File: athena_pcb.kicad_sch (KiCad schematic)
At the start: 34 parts, among them J2 Conn_01x04, SW1 SW_Push, U1 NRF5340-QKAA-R7, U2 BME280, Y1 32MHz, Y2 32.768kHz

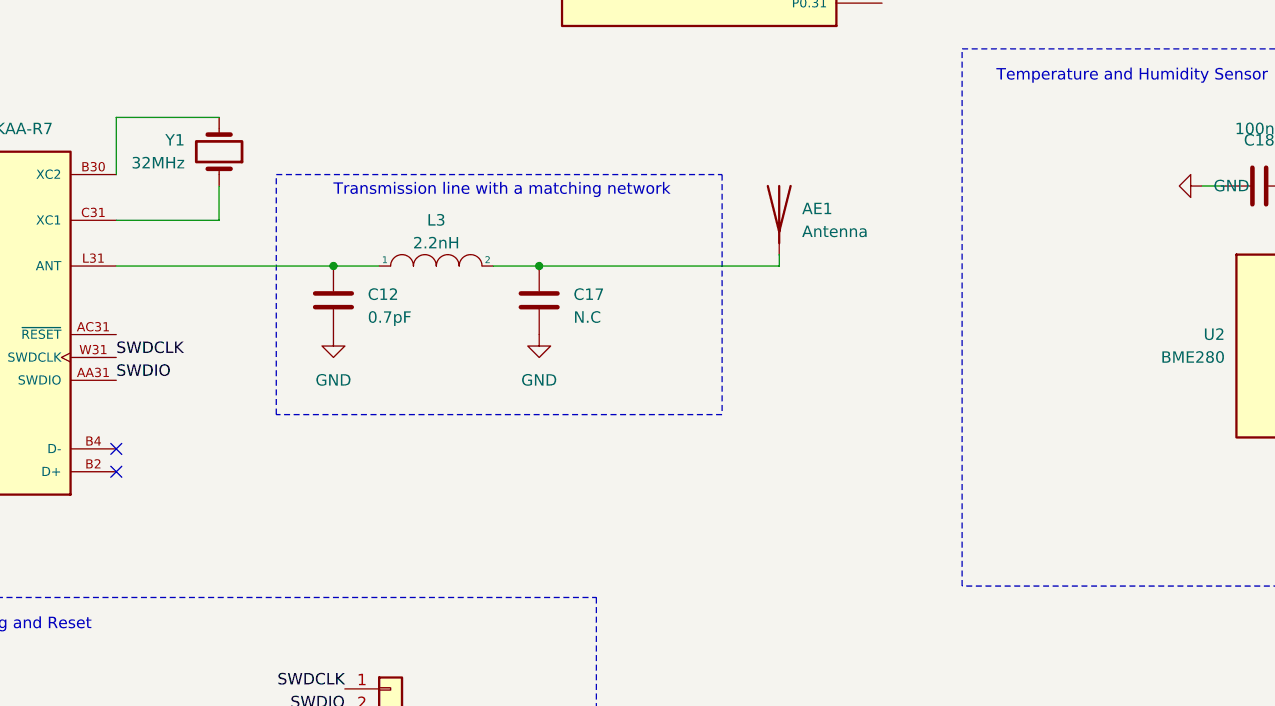
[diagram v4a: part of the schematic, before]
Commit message: Adapted PCB antenna footprint to use polygon, Workaroung for schematic symbol
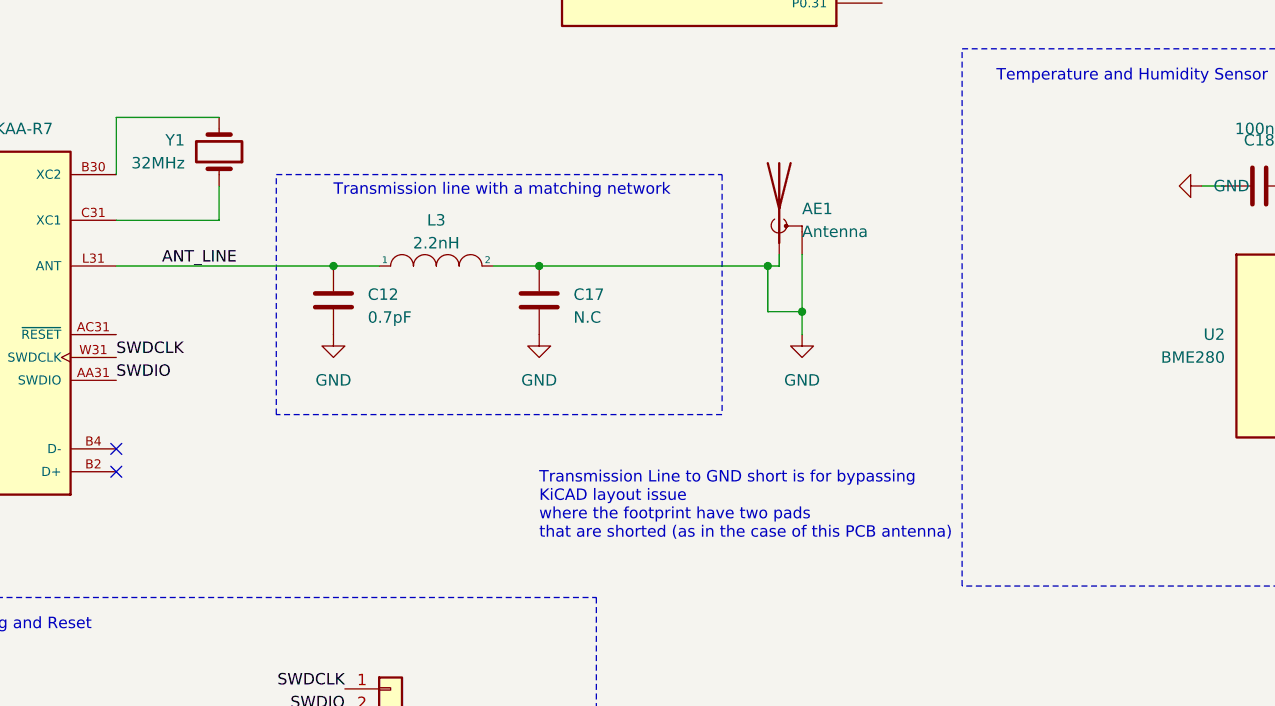
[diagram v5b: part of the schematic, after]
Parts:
- AE1: footprint RF_Antenna:Texas_SWRA117D_2.4GHz_Left -> RF_Antenna:Texas_SWRA117D_2.4GHz_Right; symbol Device:Antenna -> Device:Antenna_Shield
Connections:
- net GND: now also AE1.1 (A), AE1.2 (Shield), C17.1, L3.2
- net ANT_LINE: now reaches C12.1, L3.1, U1.L31 (ANT)
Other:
- note added: "Transmission Line to GND short is for bypassing KiCAD layout issue where the footprint have two pads that are shorted (as in the case of this PCB antenna)"
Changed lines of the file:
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@@
   (junction (at 52.07 40.64) (diameter 0) (color 0 0 0 0)
   )
+  (junction (at 191.77 133.35) (diameter 0) (color 0 0 0 0)
+  )
   (junction (at 111.76 27.94) (diameter 0) (color 0 0 0 0)
   )
@@
   )
   (junction (at 76.2 35.56) (diameter 0) (color 0 0 0 0)
+  )
+  (junction (at 187.96 128.27) (diameter 0) (color 0 0 0 0)
   )
   (junction (at 111.76 68.58) (diameter 0) (color 0 0 0 0)
@@
     (stroke (width 0) (type default))
   )
+  (wire (pts (xy 191.77 127) (xy 191.77 133.35))
+    (stroke (width 0) (type default))
+  )
   (wire (pts (xy 127 119.38) (xy 127 123.19))
     (stroke (width 0) (type default))
@@
     (stroke (width 0) (type default))
   )
+  (wire (pts (xy 187.96 133.35) (xy 191.77 133.35))
+    (stroke (width 0) (type default))
+  )
   (wire (pts (xy 69.85 68.58) (xy 69.85 69.85))
     (stroke (width 0) (type default))
@@
     (stroke (width 0) (type default))
   )
+  (wire (pts (xy 191.77 133.35) (xy 191.77 135.89))
+    (stroke (width 0) (type default))
+  )
   (wire (pts (xy 250.19 118.11) (xy 252.73 118.11))
     (stroke (width 0) (type default))
@@
     (stroke (width 0) (type default))
   )
+  (wire (pts (xy 187.96 128.27) (xy 189.23 128.27))
+    (stroke (width 0) (type default))
+  )
+  (wire (pts (xy 187.96 128.27) (xy 187.96 133.35))
+    (stroke (width 0) (type default))
+  )
   (wire (pts (xy 232.41 85.09) (xy 228.6 85.09))
     (stroke (width 0) (type default))
@@
     (stroke (width 0) (type default))
   )
-  (wire (pts (xy 162.56 128.27) (xy 189.23 128.27))
+  (wire (pts (xy 162.56 128.27) (xy 187.96 128.27))
     (stroke (width 0) (type default))
   )
@@
     (effects (font (size 1.27 1.27)) (justify left bottom))
   )
+  (text "Transmission Line to GND short is for bypassing\nKiCAD layout issue\nwhere the footprint have two pads\nthat are shorted (as in the case of this PCB antenna)\n"
+    (at 162.56 158.75 0)
+    (effects (font (size 1.27 1.27)) (justify left bottom))
+  )
   (label "SDO" (at 265.43 129.54 0) (fields_autoplaced)
     (effects (font (size 1.27 1.27)) (justify left bottom))
@@
   )
   (label "P0.02" (at 200.66 25.4 0) (fields_autoplaced)
+    (effects (font (size 1.27 1.27)) (justify left bottom))
+  )
+  (label "ANT_LINE" (at 120.65 128.27 0) (fields_autoplaced)
     (effects (font (size 1.27 1.27)) (justify left bottom))
   )
@@
         (path "/fadb6411-1081-41a3-ba72-837bcce93ee0"
           (reference "U2") (unit 1)
+        )
+      )
+    )
+  )
+  (symbol (lib_id "power:GND") (at 191.77 135.89 0) (unit 1)
+    (in_bom yes) (on_board yes) (dnp no) (fields_autoplaced)
+    (property "Reference" "#PWR06" (at 191.77 142.24 0)
+      (effects (font (size 1.27 1.27)) hide)
+    )
+    (property "Value" "GND" (at 191.77 140.97 0)
+      (effects (font (size 1.27 1.27)))
+    )
+    (property "Footprint" "" (at 191.77 135.89 0)
+      (effects (font (size 1.27 1.27)) hide)
+    )
+    (property "Datasheet" "" (at 191.77 135.89 0)
+      (effects (font (size 1.27 1.27)) hide)
+    )
+    (pin "1")
+    (instances
+      (project "athena_pcb"
+        (path "/fadb6411-1081-41a3-ba72-837bcce93ee0"
+          (reference "#PWR06") (unit 1)
         )
       )
@@
     )
   )
-  (symbol (lib_id "Device:Antenna") (at 189.23 121.92 0) (unit 1)
+  (symbol (lib_id "Device:Antenna_Shield") (at 189.23 121.92 0) (unit 1)
     (in_bom yes) (on_board yes) (dnp no) (fields_autoplaced)
     (property "Reference" "AE1" (at 191.77 121.92 0)
@@
       (effects (font (size 1.27 1.27)) (justify left))
     )
-    (property "Footprint" "RF_Antenna:Texas_SWRA117D_2.4GHz_Left" (at 189.23 121.92 0)
-      (effects (font (size 1.27 1.27)) hide)
-    )
-    (property "Datasheet" "~" (at 189.23 121.92 0)
-      (effects (font (size 1.27 1.27)) hide)
-    )
-    (pin "1")
-    (instances
-      (project "athena_pcb"
+    (property "Footprint" "RF_Antenna:Texas_SWRA117D_2.4GHz_Right" (at 189.23 119.38 0)
+      (effects (font (size 1.27 1.27)) hide)
+    )
+    (property "Datasheet" "~" (at 189.23 119.38 0)
+      (effects (font (size 1.27 1.27)) hide)
+    )
+    (pin "1")
+    (pin "2")
+    (instances
+      (project "athena_pcb"

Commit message: Added proper Y1 symbol and footprint
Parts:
- removed Y1: 32MHz, Crystal:Crystal_SMD_2016-4Pin_2.0x1.6mm, symbol Device:Crystal
- added Y1: 32MHz, XRCGB32M000F1H19R0:OSC_XRCGB32M000F1H19R0, symbol XRCGB32M000F1H19R0:XRCGB32M000F1H19R0
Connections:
- net at U1.C31 (XC1): now also Y1.3
- net at U1.B30 (XC2): now also Y1.1
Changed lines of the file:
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@@
-    (stroke (width 0) (type default))
-  )
-  (wire (pts (xy 127 119.38) (xy 127 123.19))
     (stroke (width 0) (type default))
   )
@@
     (stroke (width 0) (type default))
   )
+  (wire (pts (xy 242.57 86.36) (xy 242.57 83.82))
+    (stroke (width 0) (type default))
+  )
+  (wire (pts (xy 111.76 68.58) (xy 111.76 71.12))
+    (stroke (width 0) (type default))
+  )
+  (wire (pts (xy 60.96 45.72) (xy 76.2 45.72))
+    (stroke (width 0) (type default))
+  )
+  (wire (pts (xy 187.96 128.27) (xy 189.23 128.27))
+    (stroke (width 0) (type default))
+  )
+  (wire (pts (xy 187.96 128.27) (xy 187.96 133.35))
+    (stroke (width 0) (type default))
+  )
+  (wire (pts (xy 232.41 85.09) (xy 228.6 85.09))
+    (stroke (width 0) (type default))
+  )
+  (wire (pts (xy 236.22 119.38) (xy 238.76 119.38))
+    (stroke (width 0) (type default))
+  )
+  (wire (pts (xy 20.32 25.4) (xy 20.32 27.94))
+    (stroke (width 0) (type default))
+  )
+  (wire (pts (xy 261.62 119.38) (xy 264.16 119.38))
+    (stroke (width 0) (type default))
+  )
+  (wire (pts (xy 250.19 152.4) (xy 252.73 152.4))
+    (stroke (width 0) (type default))
+  )
+  (wire (pts (xy 139.7 128.27) (xy 144.78 128.27))
+    (stroke (width 0) (type default))
+  )
+  (wire (pts (xy 162.56 128.27) (xy 187.96 128.27))
+    (stroke (width 0) (type default))
+  )
   (wire (pts (xy 115.57 111.76) (xy 127 111.76))
     (stroke (width 0) (type default))
   )
-  (wire (pts (xy 242.57 86.36) (xy 242.57 83.82))
-    (stroke (width 0) (type default))
-  )
-  (wire (pts (xy 111.76 68.58) (xy 111.76 71.12))
-    (stroke (width 0) (type default))
-  )
-  (wire (pts (xy 60.96 45.72) (xy 76.2 45.72))
-    (stroke (width 0) (type default))
-  )
-  (wire (pts (xy 187.96 128.27) (xy 189.23 128.27))
-    (stroke (width 0) (type default))
-  )
-  (wire (pts (xy 187.96 128.27) (xy 187.96 133.35))
-    (stroke (width 0) (type default))
-  )
-  (wire (pts (xy 232.41 85.09) (xy 228.6 85.09))
-    (stroke (width 0) (type default))
-  )
-  (wire (pts (xy 236.22 119.38) (xy 238.76 119.38))
-    (stroke (width 0) (type default))
-  )
-  (wire (pts (xy 20.32 25.4) (xy 20.32 27.94))
-    (stroke (width 0) (type default))
-  )
-  (wire (pts (xy 261.62 119.38) (xy 264.16 119.38))
-    (stroke (width 0) (type default))
-  )
-  (wire (pts (xy 250.19 152.4) (xy 252.73 152.4))
-    (stroke (width 0) (type default))
-  )
-  (wire (pts (xy 139.7 128.27) (xy 144.78 128.27))
-    (stroke (width 0) (type default))
-  )
-  (wire (pts (xy 162.56 128.27) (xy 187.96 128.27))
-    (stroke (width 0) (type default))
-  )
   (wire (pts (xy 68.58 55.88) (xy 76.2 55.88))
     (stroke (width 0) (type default))
@@
   )
   (wire (pts (xy 252.73 119.38) (xy 252.73 121.92))
+    (stroke (width 0) (type default))
+  )
+  (wire (pts (xy 127 121.92) (xy 127 123.19))
     (stroke (width 0) (type default))
   )
@@
     )
   )
+  (symbol (lib_id "XRCGB32M000F1H19R0:XRCGB32M000F1H19R0") (at 127 116.84 270) (unit 1)
+    (in_bom yes) (on_board yes) (dnp no) (fields_autoplaced)
+    (property "Reference" "Y1" (at 130.81 116.205 90)
+      (effects (font (size 1.27 1.27)) (justify left))
+    )
+    (property "Value" "32MHz" (at 130.81 118.745 90)
+      (effects (font (size 1.27 1.27)) (justify left))
+    )
+    (property "Footprint" "XRCGB32M000F1H19R0:OSC_XRCGB32M000F1H19R0" (at 127 116.84 0)
+      (effects (font (size 1.27 1.27)) (justify bottom) hide)
+    )
+    (property "Datasheet" "" (at 127 116.84 0)
+      (effects (font (size 1.27 1.27)) hide)
+    )
+    (property "MANUFACTURER" "Murata Electronics" (at 127 116.84 0)
+      (effects (font (size 1.27 1.27)) (justify bottom) hide)
+    )
+    (property "PARTREV" "N/A" (at 127 116.84 0)
+      (effects (font (size 1.27 1.27)) (justify bottom) hide)
+    )
+    (property "MAXIMUM_PACKAGE_HEIGHT" "0.7 mm" (at 127 116.84 0)
+      (effects (font (size 1.27 1.27)) (justify bottom) hide)
+    )
+    (property "STANDARD" "Manufacturer Recommendations" (at 127 116.84 0)
+      (effects (font (size 1.27 1.27)) (justify bottom) hide)
+    )
+    (pin "1")
+    (pin "3")
+    (instances
+      (project "athena_pcb"
+        (path "/fadb6411-1081-41a3-ba72-837bcce93ee0"
+          (reference "Y1") (unit 1)
+        )
+      )
+    )
+  )
   (symbol (lib_id "NRF5340-QKAA-R7:NRF5340-QKAA-R7") (at 180.34 58.42 0) (mirror y) (unit 3)
     (in_bom yes) (on_board yes) (dnp no) (fields_autoplaced)
@@
         )
       )
-    )
-  )
-  (symbol (lib_id "Device:Crystal") (at 127 115.57 270) (mirror x) (unit 1)
-    (in_bom yes) (on_board yes) (dnp no) (fields_autoplaced)
-    (property "Reference" "Y1" (at 123.19 114.2999 90)
-      (effects (font (size 1.27 1.27)) (justify right))
-    )
-    (property "Value" "32MHz" (at 123.19 116.8399 90)
-      (effects (font (size 1.27 1.27)) (justify right))
-    )
-    (property "Footprint" "Crystal:Crystal_SMD_2016-4Pin_2.0x1.6mm" (at 127 115.57 0)
-      (effects (font (size 1.27 1.27)) hide)
-    )
-    (property "Datasheet" "~" (at 127 115.57 0)
-      (effects (font (size 1.27 1.27)) hide)
-    )
-    (pin "1")
-    (pin "2")
-    (instances
-      (project "athena_pcb"
-        (path "/fadb6411-1081-41a3-ba72-837bcce93ee0"
-          (reference "Y1") (unit 1)
-        )
-      )

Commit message: Polishing layout
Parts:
- added TP3, TP4: TestPoint, TestPoint:TestPoint_Pad_D1.0mm, symbol Connector:TestPoint
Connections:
- net CSB: now also TP4.1
- net SDO: now also TP3.1
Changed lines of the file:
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@@
+    (stroke (width 0) (type default))
+  )
+  (wire (pts (xy 228.6 95.25) (xy 228.6 93.98))
     (stroke (width 0) (type default))
   )
@@
     (stroke (width 0) (type default))
   )
+  (wire (pts (xy 247.65 95.25) (xy 243.84 95.25))
+    (stroke (width 0) (type default))
+  )
   (wire (pts (xy 31.75 101.6) (xy 31.75 104.14))
     (stroke (width 0) (type default))
@@
     (stroke (width 0) (type default))
   )
+  (wire (pts (xy 228.6 95.25) (xy 233.68 95.25))
+    (stroke (width 0) (type default))
+  )
   (wire (pts (xy 261.62 119.38) (xy 264.16 119.38))
+    (stroke (width 0) (type default))
+  )
+  (wire (pts (xy 243.84 95.25) (xy 243.84 92.71))
     (stroke (width 0) (type default))
   )
@@
     (effects (font (size 1.27 1.27)) (justify left bottom))
   )
+  (label "CSB" (at 247.65 95.25 0) (fields_autoplaced)
+    (effects (font (size 1.27 1.27)) (justify left bottom))
+  )
   (label "P0.02" (at 200.66 25.4 0) (fields_autoplaced)
     (effects (font (size 1.27 1.27)) (justify left bottom))
@@
   )
   (label "SWDCLK" (at 115.57 138.43 0) (fields_autoplaced)
+    (effects (font (size 1.27 1.27)) (justify left bottom))
+  )
+  (label "SDO" (at 233.68 95.25 0) (fields_autoplaced)
     (effects (font (size 1.27 1.27)) (justify left bottom))
   )
@@
     )
   )
+  (symbol (lib_id "Connector:TestPoint") (at 243.84 92.71 0) (unit 1)
+    (in_bom yes) (on_board yes) (dnp no) (fields_autoplaced)
+    (property "Reference" "TP4" (at 246.38 88.773 0)
+      (effects (font (size 1.27 1.27)) (justify left))
+    )
+    (property "Value" "TestPoint" (at 246.38 91.313 0)
+      (effects (font (size 1.27 1.27)) (justify left))
+    )
+    (property "Footprint" "TestPoint:TestPoint_Pad_D1.0mm" (at 248.92 92.71 0)
+      (effects (font (size 1.27 1.27)) hide)
+    )
+    (property "Datasheet" "~" (at 248.92 92.71 0)
+      (effects (font (size 1.27 1.27)) hide)
+    )
+    (pin "1")
+    (instances
+      (project "athena_pcb"
+        (path "/fadb6411-1081-41a3-ba72-837bcce93ee0"
+          (reference "TP4") (unit 1)
+        )
+      )
+    )
+  )
   (symbol (lib_id "Device:C") (at 257.81 119.38 90) (unit 1)
     (in_bom yes) (on_board yes) (dnp no)
@@
         )
       )
+    )
+  )
+  (symbol (lib_id "Connector:TestPoint") (at 228.6 93.98 0) (unit 1)
+    (in_bom yes) (on_board yes) (dnp no) (fields_autoplaced)
+    (property "Reference" "TP3" (at 231.14 90.043 0)
+      (effects (font (size 1.27 1.27)) (justify left))
+    )
+    (property "Value" "TestPoint" (at 231.14 92.583 0)
+      (effects (font (size 1.27 1.27)) (justify left))
+    )
+    (property "Footprint" "TestPoint:TestPoint_Pad_D1.0mm" (at 233.68 93.98 0)
+      (effects (font (size 1.27 1.27)) hide)
+    )
+    (property "Datasheet" "~" (at 233.68 93.98 0)
+      (effects (font (size 1.27 1.27)) hide)
+    )
+    (pin "1")
+    (instances
+      (project "athena_pcb"
+        (path "/fadb6411-1081-41a3-ba72-837bcce93ee0"
+          (reference "TP3") (unit 1)
+        )
+      )
